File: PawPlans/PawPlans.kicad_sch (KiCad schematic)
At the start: 7 parts

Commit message: Completely revamped the schematic and PCB, cleaned up project files
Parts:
- removed LOAD-CELL1: SEN-13879, Parts:SPARKFUN_SEN-13879, symbol SEN-13879:SEN-13879
- removed PROXIMITY-SENSOR1: ~, Ultrasonic Sensor HC-SR04:HC-SR04_FOOTPRINT, symbol Ultrasonic Sensor HC-SR04:HC-SR04
- added LOADCELL1: ~, SparkFun_HX711_Load_Cell_Amplifier_SEN-13879:SPARKFUN-CONNECTORS_1X05, symbol SparkFun_HX711_Load_Cell:SPARKFUN-CONNECTORS_M05PTH
- added PROXIMITY1: ~, Ultrasonic_Proximity_Sensor_HC-SR04:HC-SR04_FOOTPRINT, symbol Ultrasonic Sensor HC-SR04:HC-SR04
- BUZZER1: footprint Parts:XTAL_PS1240P02BT_TDK -> TDK_Piezo_Buzzer_PS1240P02BT:XTAL_PS1240P02BT_TDK
- DISPLAY1: renamed from OLED-BREAKOUT1; footprint Qwiic_OLED_1.3in:SPARKX_1X04_NO_SILK -> SparkFun_Qwiic_OLED_128x64_LCD-23453:SPARKX_1X04
- JOYSTICK1: footprint Parts:1X05 -> Adafruit_Joystick_512:PINHEAD_1X05
- MCUKIT1: renamed from WIFI-DEVKIT1; footprint Espressif:ESP32-C6-DevKitC-1 -> Espressif_ESP32:ESP32-C6-DevKitC-1
- SERVO1: footprint Motors:Vybronics_VZ30C1T8219732L -> Connector_PinHeader_2.00mm:PinHeader_1x03_P2.00mm_Vertical
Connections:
- net 3V3: now also LOADCELL1.1
- net GND: now also LOADCELL1.5, PROXIMITY1.GND
- net VCC: now also LOADCELL1.2, PROXIMITY1.VCC (5V)
- net DSPSDA: now reaches DISPLAY1.3 (SDA), MCUKIT1.4 (GPIO5/MTDI)
- net DSPSCL: now reaches DISPLAY1.4 (SCL), MCUKIT1.5 (GPIO6)
- net SRVPWM: now reaches MCUKIT1.22 (GPIO9/BOOT)
- net SRVPWM: now also SERVO1.1 (PWM)
- net at MCUKIT1.12 (GPIO2): no longer SERVO1.1 (PWM)
- net JOYX: now reaches JOYSTICK1.2
- net JOYX: now also MCUKIT1.28 (GPIO23); no longer MCUKIT1.31 (GPIO16/U0TXD)
- net at MCUKIT1.30 (GPIO17/U0RXD): no longer JOYSTICK1.3
- net at MCUKIT1.29 (GPIO15/JTAG): no longer JOYSTICK1.4
- net at MCUKIT1.19 (GPIO12/USB_D-): no longer BUZZER1.1
- net LDCCLK: now reaches MCUKIT1.6 (GPIO7)
- net LDCCLK: now also LOADCELL1.4
- net LDCDAT: now reaches MCUKIT1.7 (GPIO0)
- net LDCDAT: now also LOADCELL1.3
- net PRXTRG: now reaches MCUKIT1.24 (GPIO19)
- net PRXTRG: now also PROXIMITY1.TRIG
- net PRXECH: now reaches MCUKIT1.25 (GPIO20)
- net PRXECH: now also PROXIMITY1.ECHO
- net JOYSEL: now reaches MCUKIT1.26 (GPIO21)
- net JOYSEL: now also JOYSTICK1.4
- net JOYY: now reaches MCUKIT1.27 (GPIO22)
- net JOYY: now also JOYSTICK1.3
- new net PZOSIG: BUZZER1.1, MCUKIT1.31 (GPIO16/U0TXD)
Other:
- note removed: "0.1"
- note removed: "2025-02-27"
- note removed: "Automatic Pet Feeder"
- note removed: "Team Happy Pets Automatic Pet Feeder Sriram Vishnubhotla, Logan Swoyer"
- company: (none) -> Clemson University
- title: (none) -> PawPlans - Automatic Pet Feeder
- moved on the sheet: BUZZER1A, DISPLAY1, JOYSTICK1, MCUKIT1, SERVO1

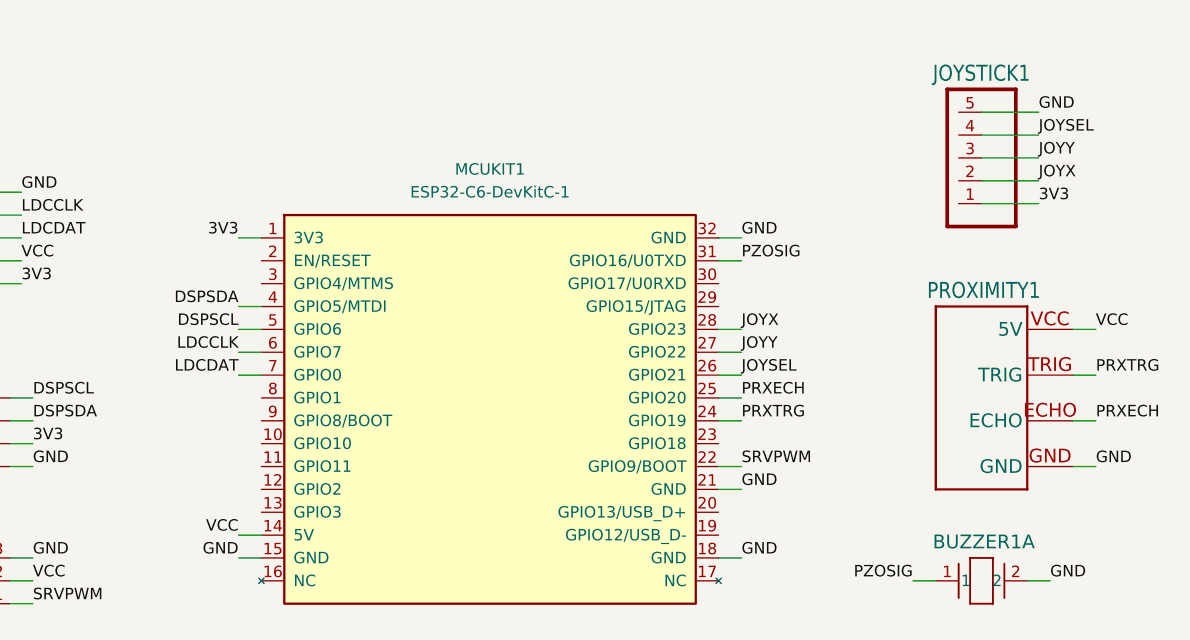
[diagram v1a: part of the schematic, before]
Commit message: Adjusted the board, switched TDK piezo buzzer for a Murata
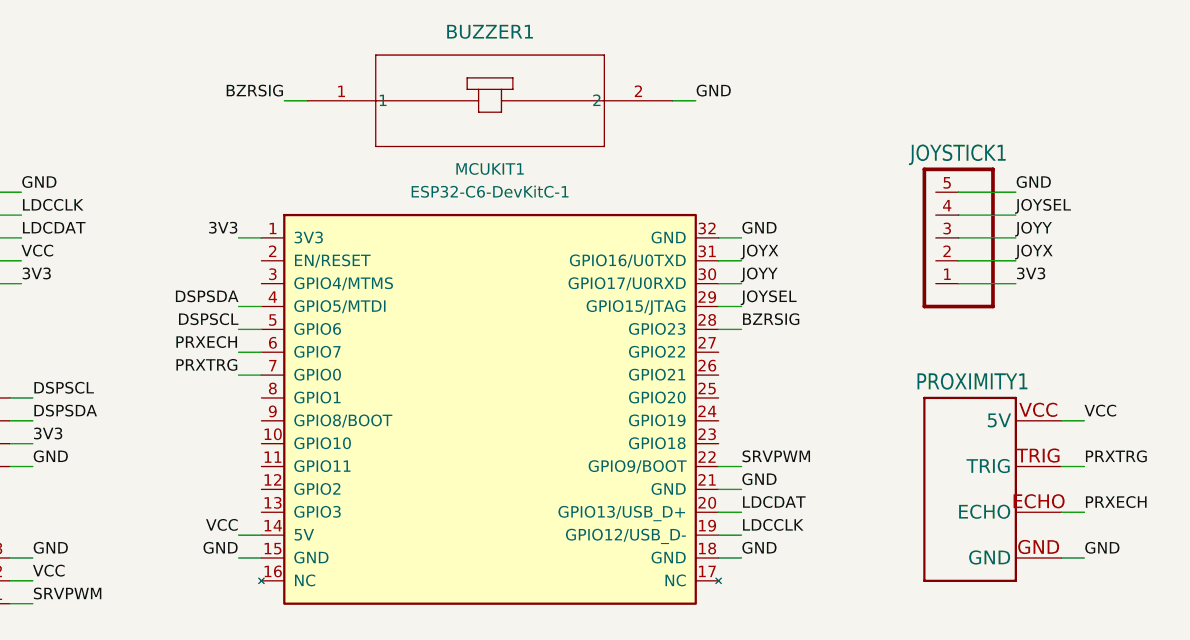
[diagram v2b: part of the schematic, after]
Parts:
- removed BUZZER1: PS1240P02BT, TDK_Piezo_Buzzer_PS1240P02BT:XTAL_PS1240P02BT_TDK, symbol PS1240P02BT:PS1240P02BT
- added BUZZER1: PKMCS0909E4000-R1, Murata_SMD_Buzzer_PKMCS0909E4000-R1:PKMCS0909E4000-R1_MUR, symbol Murata_SMD_Buzzer_PKMCS0909E4000-R1:PKMCS0909E4000-R1
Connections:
- net PZOSIG is gone; now on net JOYX: MCUKIT1.31 (GPIO16/U0TXD)
- net GND: now also BUZZER1.2
- net JOYSEL: now also MCUKIT1.29 (GPIO15/JTAG); no longer MCUKIT1.26 (GPIO21)
- net JOYX: no longer MCUKIT1.28 (GPIO23)
- net JOYY: now also MCUKIT1.30 (GPIO17/U0RXD); no longer MCUKIT1.27 (GPIO22)
- net LDCCLK: now also MCUKIT1.19 (GPIO12/USB_D-); no longer MCUKIT1.6 (GPIO7)
- net LDCDAT: now also MCUKIT1.20 (GPIO13/USB_D+); no longer MCUKIT1.7 (GPIO0)
- net PRXECH: now also MCUKIT1.6 (GPIO7); no longer MCUKIT1.25 (GPIO20)
- net PRXTRG: now also MCUKIT1.7 (GPIO0); no longer MCUKIT1.24 (GPIO19)
- new net BZRSIG: BUZZER1.1, MCUKIT1.28 (GPIO23)
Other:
- moved on the sheet: JOYSTICK1, PROXIMITY1

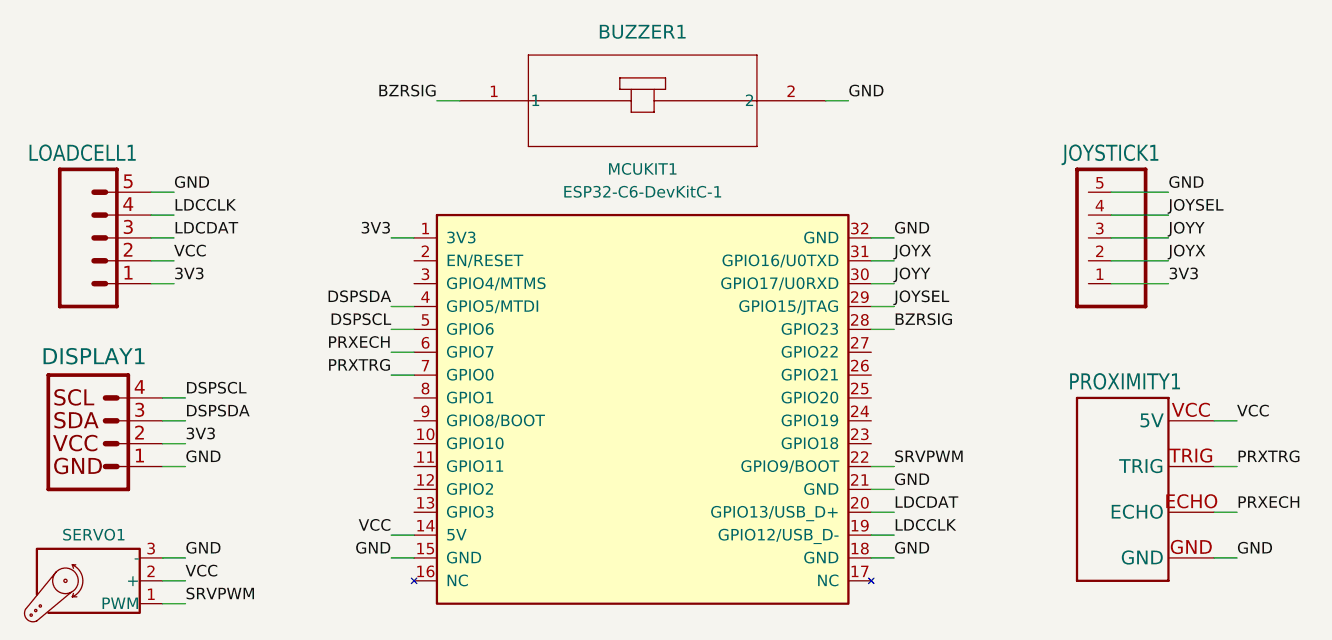
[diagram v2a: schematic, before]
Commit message: Reworked hardware (centered around M5Stack's DinMeter, ESP32), adjusted board and schematic
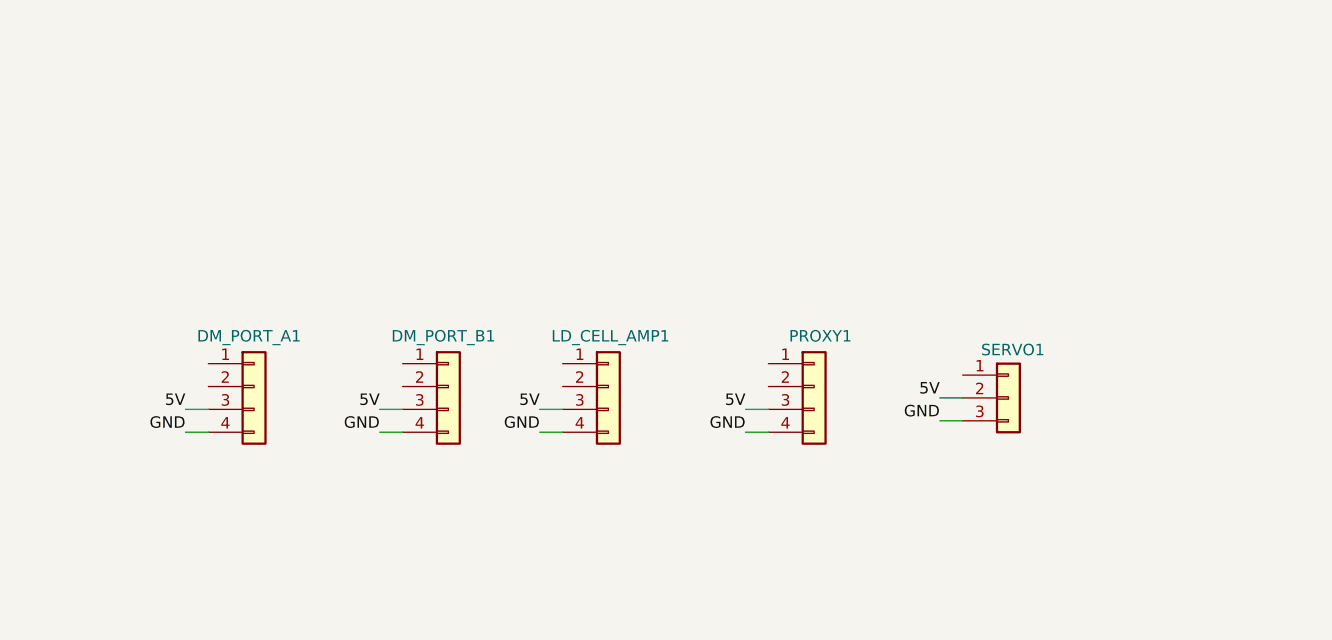
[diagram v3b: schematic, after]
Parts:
- removed BUZZER1: PKMCS0909E4000-R1, Murata_SMD_Buzzer_PKMCS0909E4000-R1:PKMCS0909E4000-R1_MUR, symbol Murata_SMD_Buzzer_PKMCS0909E4000-R1:PKMCS0909E4000-R1
- removed DISPLAY1: ~, SparkFun_Qwiic_OLED_128x64_LCD-23453:SPARKX_1X04, symbol Qwiic_OLED_1.3in:I2C_STANDARD_NO_SILK
- removed JOYSTICK1: JOYSTICK-512, Adafruit_Joystick_512:PINHEAD_1X05, symbol Joystick-512:pinhead_PINHD-1X5
- removed LOADCELL1: ~, SparkFun_HX711_Load_Cell_Amplifier_SEN-13879:SPARKFUN-CONNECTORS_1X05, symbol SparkFun_HX711_Load_Cell:SPARKFUN-CONNECTORS_M05PTH
- removed MCUKIT1: ESP32-C6-DevKitC-1, Espressif_ESP32:ESP32-C6-DevKitC-1, symbol Espressif:ESP32-C6-DevKitC-1
- removed PROXIMITY1: ~, Ultrasonic_Proximity_Sensor_HC-SR04:HC-SR04_FOOTPRINT, symbol Ultrasonic Sensor HC-SR04:HC-SR04
- removed SERVO1: Motor_Servo, Connector_PinHeader_2.00mm:PinHeader_1x03_P2.00mm_Vertical, symbol Motor:Motor_Servo
- added DM_PORT_A1, DM_PORT_B1, LD_CELL_AMP1, PROXY1: Conn_01x04, Connector_PinHeader_2.54mm:PinHeader_1x04_P2.54mm_Vertical, symbol Connector_Generic:Conn_01x04
- added SERVO1: Conn_01x03, Connector_PinHeader_2.54mm:PinHeader_1x03_P2.54mm_Vertical, symbol Connector_Generic:Conn_01x03
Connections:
- net GND: now also DM_PORT_A1.4 (GND), DM_PORT_B1.4 (GND), LD_CELL_AMP1.4 (GND), PROXY1.4 (GND), SERVO1.3 (GND)
- new net 5V: DM_PORT_A1.3 (5V), DM_PORT_B1.3 (5V), LD_CELL_AMP1.3 (5V), PROXY1.3 (5V), SERVO1.2 (5V)
